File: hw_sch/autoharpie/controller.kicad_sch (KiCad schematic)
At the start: 24 parts, among them J2 Conn_01x03_Socket, SW1 SW_Push, SW2 SW_Push, U1 RP2040, U2 W25Q32JVZP, Y1 Crystal

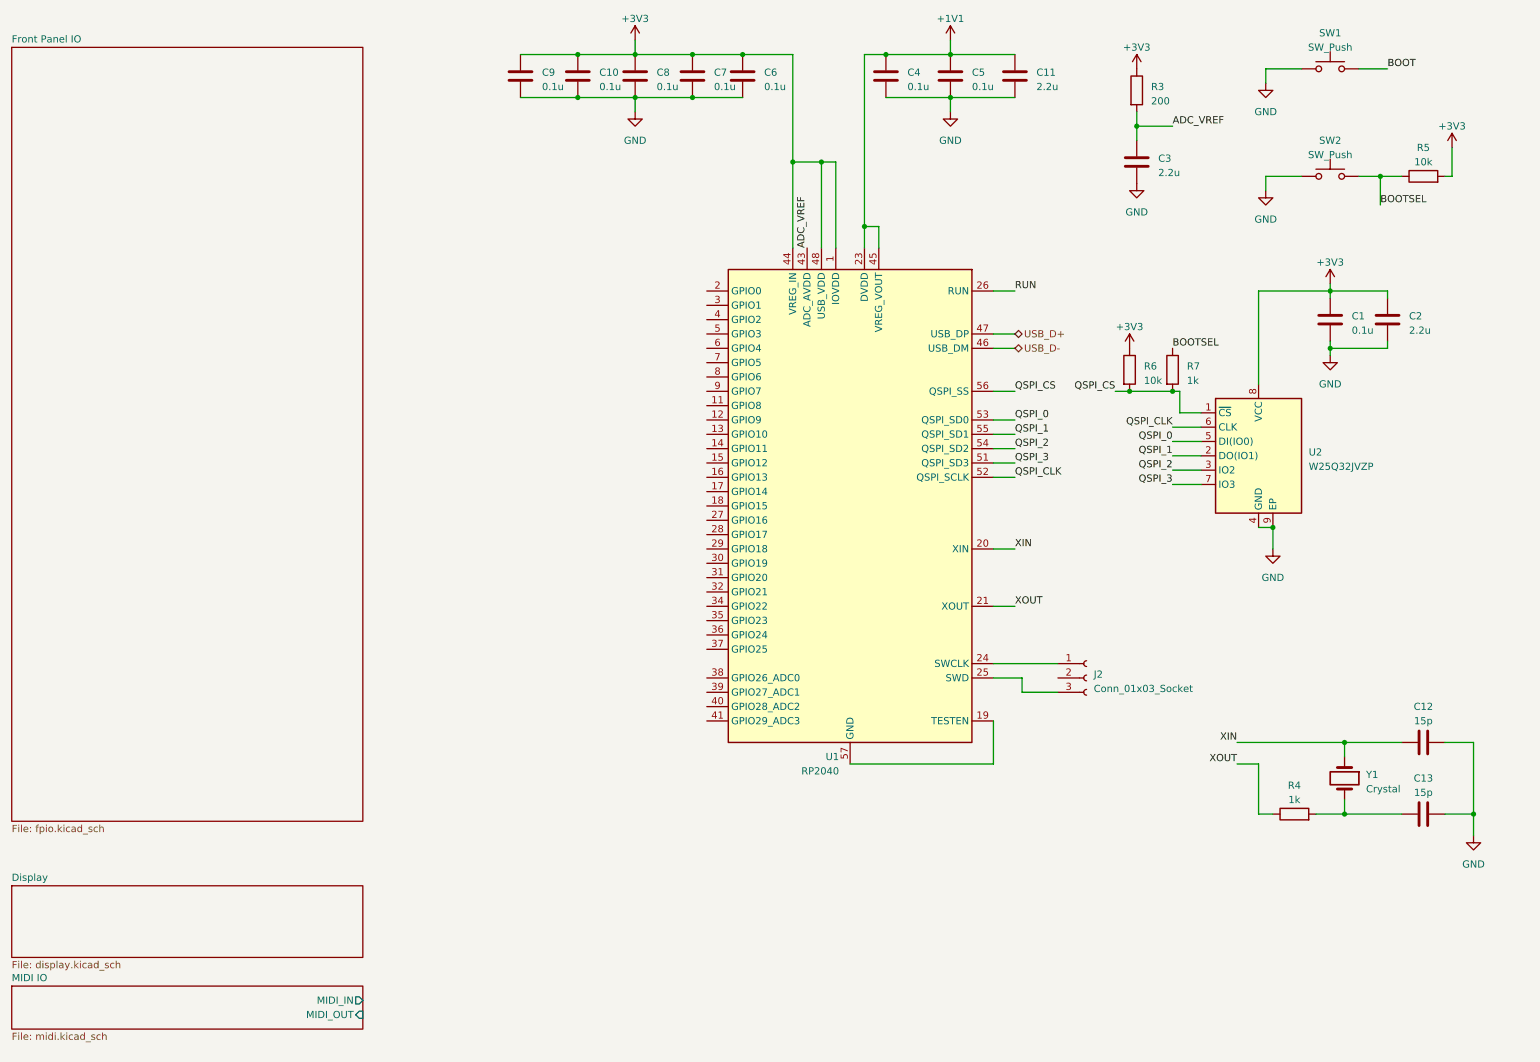
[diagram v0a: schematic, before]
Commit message: teensy mcu chip (imxrt), PSU subsystem work start
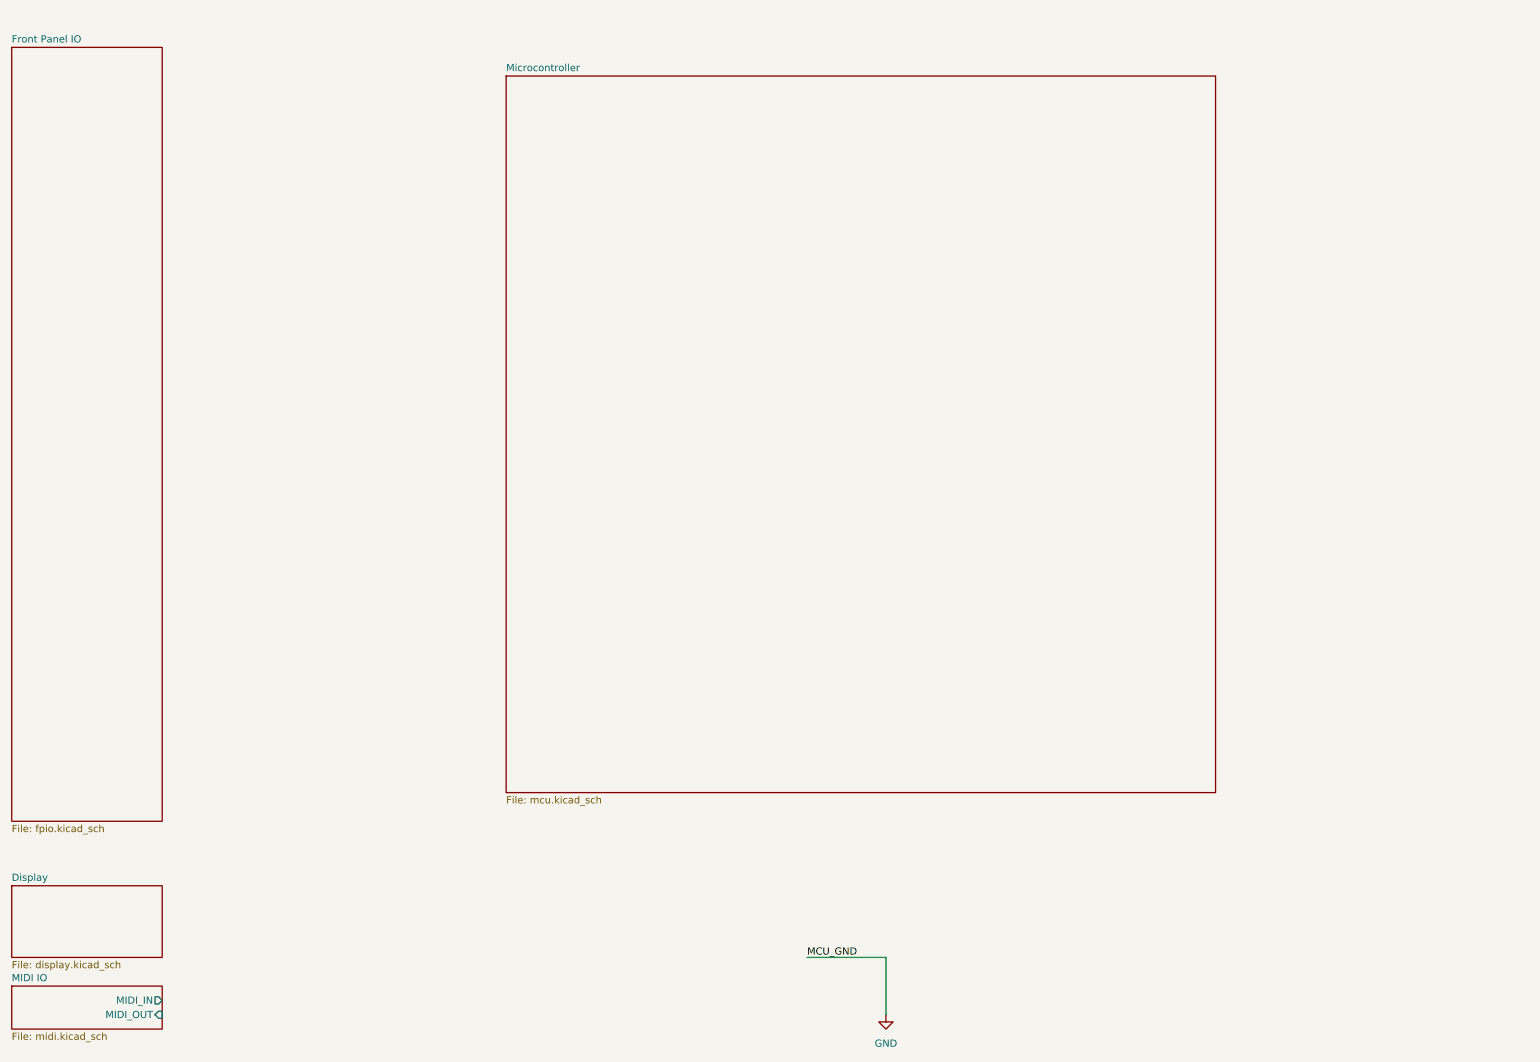
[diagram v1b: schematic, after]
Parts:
- removed C1, C10, C4, C5, C6, C7, C8, C9: 0.1u, symbol Device:C
- removed C11, C2, C3: 2.2u, symbol Device:C
- removed C12, C13: 15p, symbol Device:C
- removed J2: Conn_01x03_Socket, symbol Connector:Conn_01x03_Socket
- removed R3: 200, symbol Device:R
- removed R4, R7: 1k, symbol Device:R
- removed R5, R6: 10k, symbol Device:R
- removed SW1, SW2: SW_Push, symbol Switch:SW_Push
- removed U1: RP2040, Package_DFN_QFN:QFN-56-1EP_7x7mm_P0.4mm_EP3.2x3.2mm, symbol MCU_RaspberryPi:RP2040
- removed U2: W25Q32JVZP, Package_SON:WSON-8-1EP_6x5mm_P1.27mm_EP3.4x4.3mm, symbol Memory_Flash:W25Q32JVZP
- removed Y1: Crystal, symbol Device:Crystal
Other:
- added sheet Microcontroller (mcu.kicad_sch)

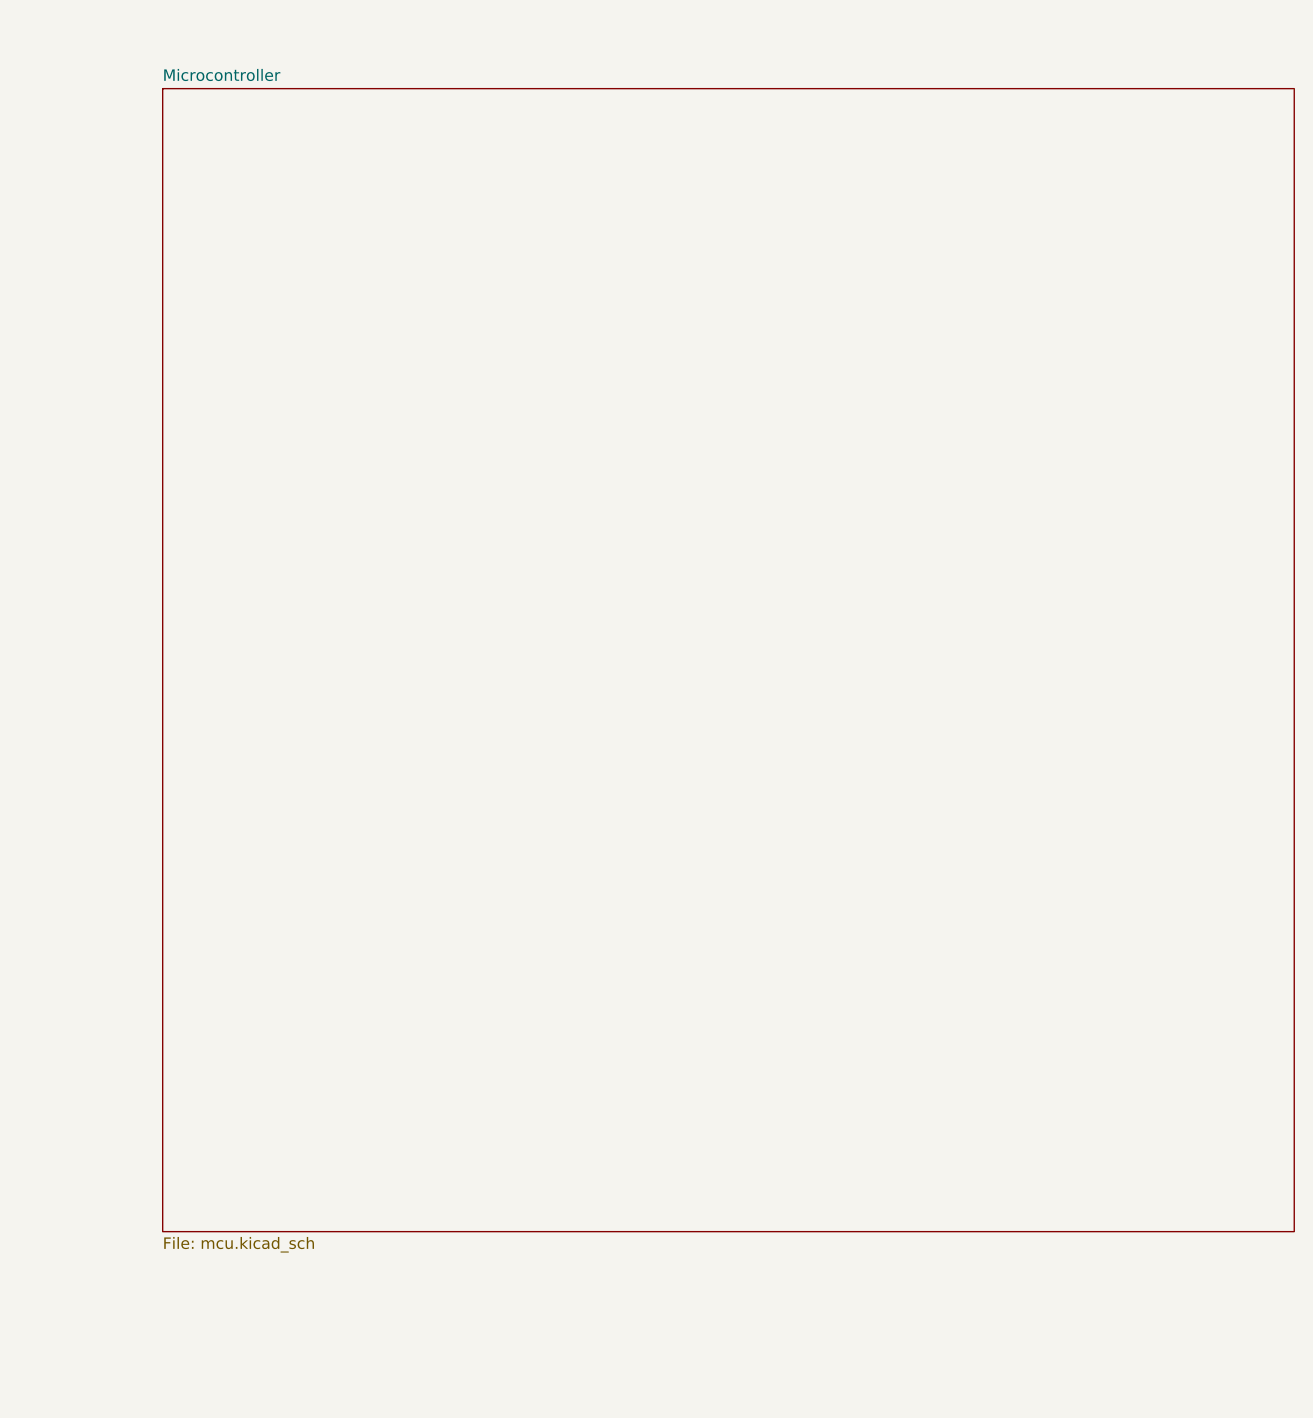
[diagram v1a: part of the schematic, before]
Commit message: switch to teensy reduce pins
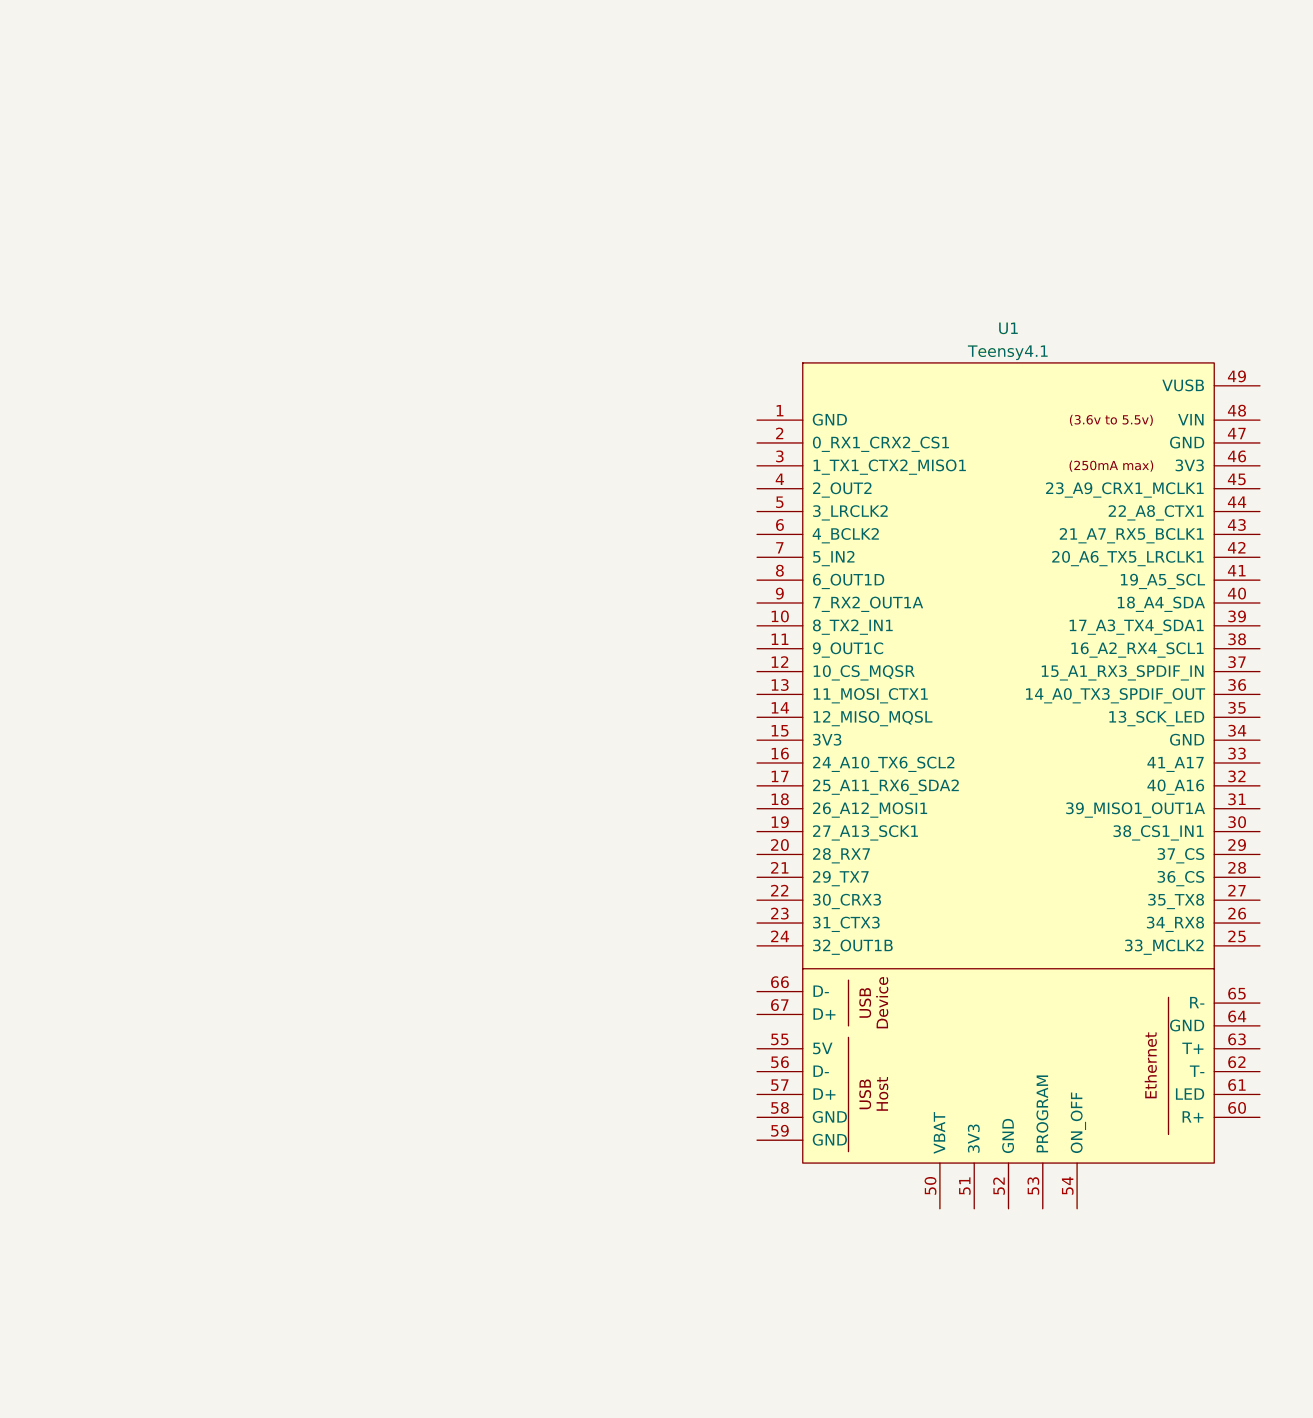
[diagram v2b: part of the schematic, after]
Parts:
- added U1: Teensy4.1, symbol teensy:Teensy4.1
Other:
- removed sheet Microcontroller
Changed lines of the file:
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@@
     (effects (font (size 1.27 1.27)) (justify left bottom))
+  )
+  (symbol (lib_id "teensy:Teensy4.1") (at 199.39 115.57 0) (unit 1)
+    (in_bom yes) (on_board yes) (dnp no) (fields_autoplaced)
+    (property "Reference" "U1" (at 199.39 50.8 0)
+      (effects (font (size 1.27 1.27)))
+    )
+    (property "Value" "Teensy4.1" (at 199.39 53.34 0)
+      (effects (font (size 1.27 1.27)))
+    )
+    (property "Footprint" "" (at 189.23 105.41 0)
+      (effects (font (size 1.27 1.27)) hide)
+    )
+    (property "Datasheet" "" (at 189.23 105.41 0)
+      (effects (font (size 1.27 1.27)) hide)
+    )
+    (pin "10")
+    (pin "11")
+    (pin "12")
+    (pin "13")
+    (pin "14")
+    (pin "15")
+    (pin "16")
+    (pin "17")
+    (pin "18")
+    (pin "19")
+    (pin "20")
+    (pin "21")
+    (pin "22")
+    (pin "23")
+    (pin "24")
+    (pin "25")
+    (pin "26")
+    (pin "27")
+    (pin "28")
+    (pin "29")
+    (pin "30")
+    (pin "31")
+    (pin "32")
+    (pin "33")
+    (pin "35")
+    (pin "36")
+    (pin "37")
+    (pin "38")
+    (pin "39")
+    (pin "40")
+    (pin "41")
+    (pin "42")
+    (pin "43")
+    (pin "44")
+    (pin "45")
+    (pin "46")
+    (pin "47")
+    (pin "48")
+    (pin "49")
+    (pin "5")
+    (pin "50")
+    (pin "51")
+    (pin "52")
+    (pin "53")
+    (pin "54")
+    (pin "55")
+    (pin "56")
+    (pin "57")
+    (pin "58")
+    (pin "59")
+    (pin "6")
+    (pin "60")
+    (pin "61")
+    (pin "62")
+    (pin "63")
+    (pin "64")
+    (pin "65")
+    (pin "66")
+    (pin "67")
+    (pin "7")
+    (pin "8")
+    (pin "9")
+    (pin "1")
+    (pin "2")
+    (pin "3")
+    (pin "34")
+    (pin "4")
+    (instances
+      (project "autoharpie"
+        (path "/f22a88c4-866b-40a0-9fc2-96344be0ec71/4d9f1d6c-21ab-45cf-b058-d32e1eb1198b"
+          (reference "U1") (unit 1)
+        )
+      )
+    )
   )
   (symbol (lib_id "power:GND") (at 172.72 190.5 0) (unit 1)
@@
       )
     )
-  )
-  (sheet (at 105.41 24.13) (size 125.73 127) (fields_autoplaced)
-    (stroke (width 0.1524) (type solid))
-    (fill (color 0 0 0 0.0000))
-    (property "Sheetname" "Microcontroller" (at 105.41 23.4184 0)
-      (effects (font (size 1.27 1.27)) (justify left bottom))
-    )
-    (property "Sheetfile" "mcu.kicad_sch" (at 105.41 151.7146 0)
-      (effects (font (size 1.27 1.27)) (justify left top))
-    )
-    (instances
-      (project "autoharpie"
-        (path "/f22a88c4-866b-40a0-9fc2-96344be0ec71/4d9f1d6c-21ab-45cf-b058-d32e1eb1198b" (page "13"))
-      )
-    )

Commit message: matrix, flattening
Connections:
- net VBUS: now reaches U1.49 (VUSB)
- net USB_D-: now reaches U1.66 (D-)
- net USB_D+: now reaches U1.67 (D+)
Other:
- removed sheet Display
- removed sheet Front Panel IO
- removed sheet MIDI IO
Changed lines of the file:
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@@
 (kicad_sch (version 20230121) (generator eeschema)
   (paper "A4")
+  (wire (pts (xy 233.68 57.15) (xy 227.33 57.15))
+    (stroke (width 0) (type default))
+  )
+  (wire (pts (xy 233.68 52.07) (xy 233.68 57.15))
+    (stroke (width 0) (type default))
+  )
+  (wire (pts (xy 165.1 124.46) (xy 171.45 124.46))
+    (stroke (width 0) (type default))
+  )
   (wire (pts (xy 172.72 180.34) (xy 172.72 190.5))
     (stroke (width 0) (type default))
@@
     (stroke (width 0) (type default))
   )
+  (wire (pts (xy 165.1 127) (xy 171.45 127))
+    (stroke (width 0) (type default))
+  )
   (label "MCU_GND" (at 158.75 180.34 0) (fields_autoplaced)
     (effects (font (size 1.27 1.27)) (justify left bottom))
+  )
+  (hierarchical_label "USB_D-" (shape bidirectional) (at 165.1 124.46 180) (fields_autoplaced)
+    (effects (font (size 1.27 1.27)) (justify right))
+  )
+  (hierarchical_label "USB_D+" (shape bidirectional) (at 165.1 127 180) (fields_autoplaced)
+    (effects (font (size 1.27 1.27)) (justify right))
   )
   (symbol (lib_id "teensy:Teensy4.1") (at 199.39 115.57 0) (unit 1)
@@
     )
   )
+  (symbol (lib_id "power:VBUS") (at 233.68 52.07 0) (unit 1)
+    (in_bom yes) (on_board yes) (dnp no) (fields_autoplaced)
+    (property "Reference" "#PWR013" (at 233.68 55.88 0)
+      (effects (font (size 1.27 1.27)) hide)
+    )
+    (property "Value" "VBUS" (at 233.68 48.26 0)
+      (effects (font (size 1.27 1.27)))
+    )
+    (property "Footprint" "" (at 233.68 52.07 0)
+      (effects (font (size 1.27 1.27)) hide)
+    )
+    (property "Datasheet" "" (at 233.68 52.07 0)
+      (effects (font (size 1.27 1.27)) hide)
+    )
+    (pin "1")
+    (instances
+      (project "autoharpie"
+        (path "/f22a88c4-866b-40a0-9fc2-96344be0ec71/4d9f1d6c-21ab-45cf-b058-d32e1eb1198b"
+          (reference "#PWR013") (unit 1)
+        )
+      )
+    )
+  )
   (symbol (lib_id "power:GND") (at 172.72 190.5 0) (unit 1)
     (in_bom yes) (on_board yes) (dnp no) (fields_autoplaced)
@@
       )
     )
-  )
-  (sheet (at 17.78 167.64) (size 26.67 12.7) (fields_autoplaced)
-    (stroke (width 0.1524) (type solid))
-    (fill (color 0 0 0 0.0000))
-    (property "Sheetname" "Display" (at 17.78 166.9284 0)
-      (effects (font (size 1.27 1.27)) (justify left bottom))
-    )
-    (property "Sheetfile" "display.kicad_sch" (at 17.78 180.9246 0)
-      (effects (font (size 1.27 1.27)) (justify left top))
-    )
-    (instances
-      (project "autoharpie"
-        (path "/f22a88c4-866b-40a0-9fc2-96344be0ec71/4d9f1d6c-21ab-45cf-b058-d32e1eb1198b" (page "7"))
-      )
-    )
-  )
-  (sheet (at 17.78 19.05) (size 26.67 137.16) (fields_autoplaced)
-    (stroke (width 0.1524) (type solid))
-    (fill (color 0 0 0 0.0000))
-    (property "Sheetname" "Front Panel IO" (at 17.78 18.3384 0)
-      (effects (font (size 1.27 1.27)) (justify left bottom))
-    )
-    (property "Sheetfile" "fpio.kicad_sch" (at 17.78 156.7946 0)
-      (effects (font (size 1.27 1.27)) (justify left top))
-    )
-    (instances
-      (project "autoharpie"
-        (path "/f22a88c4-866b-40a0-9fc2-96344be0ec71/4d9f1d6c-21ab-45cf-b058-d32e1eb1198b" (page "5"))
-      )
-    )
-  )
-  (sheet (at 17.78 185.42) (size 26.67 7.62) (fields_autoplaced)
-    (stroke (width 0.1524) (type solid))
-    (fill (color 0 0 0 0.0000))
-    (property "Sheetname" "MIDI IO" (at 17.78 184.7084 0)
-      (effects (font (size 1.27 1.27)) (justify left bottom))
-    )
-    (property "Sheetfile" "midi.kicad_sch" (at 17.78 193.6246 0)
-      (effects (font (size 1.27 1.27)) (justify left top))
-    )
-    (pin "MIDI_IN" output (at 44.45 187.96 0)
-      (effects (font (size 1.27 1.27)) (justify right))
-    )
-    (pin "MIDI_OUT" input (at 44.45 190.5 0)
-      (effects (font (size 1.27 1.27)) (justify right))
-    )
-    (instances
-      (project "autoharpie"
-        (path "/f22a88c4-866b-40a0-9fc2-96344be0ec71/4d9f1d6c-21ab-45cf-b058-d32e1eb1198b" (page "6"))
-      )
-    )
